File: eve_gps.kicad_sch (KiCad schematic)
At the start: 9 parts, among them J14 BMI-S-101, J15 GNSS SMA

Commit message: Addressed comments; See issue for notes
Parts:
- removed J14: BMI-S-101, RF_Shielding:Laird_Technologies_BMI-S-101_13.66x12.70mm, symbol Device:RFShield_OnePiece
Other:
- note removed: "MURK SHIELD AND MOVE CIRCUIT COSER"
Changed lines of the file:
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@@
-		)
-	)
-	(text "MURK SHIELD AND  MOVE CIRCUIT COSER"
-		(exclude_from_sim no)
-		(at 185.674 117.602 0)
-		(effects
-			(font
-				(size 1.27 1.27)
-				(color 255 0 21 1)
-			)
 		)
 	)
@@
 					(unit 1)
 				)
-			)
-		)
-	)
-	(symbol
-		(lib_id "power:GND")
-		(at 168.91 144.78 0)
-		(unit 1)
-		(exclude_from_sim no)
-		(in_bom yes)
-		(on_board yes)
-		(dnp no)
-		(property "Reference" "#PWR0193"
-			(at 168.91 151.13 0)
-			(effects
-				(font
-					(size 1.27 1.27)
-				)
-				(hide yes)
-			)
-		)
-		(property "Value" "GND"
-			(at 168.91 148.59 0)
-			(effects
-				(font
-					(size 1.27 1.27)
-				)
-			)
-		)
-		(property "Footprint" ""
-			(at 168.91 144.78 0)
-			(effects
-				(font
-					(size 1.27 1.27)
-				)
-				(hide yes)
-			)
-		)
-		(property "Datasheet" ""
-			(at 168.91 144.78 0)
-			(effects
-				(font
-					(size 1.27 1.27)
-				)
-				(hide yes)
-			)
-		)
-		(property "Description" ""
-			(at 168.91 144.78 0)
-			(effects
-				(font
-					(size 1.27 1.27)
-				)
-				(hide yes)
-			)
-		)
-		(pin "1"
-		)
-		(instances
-			(project "rocket2-ecu"
-				(path "/02606b2c-b376-4ffb-9781-f9cea3f70994/33703977-e0e9-46ee-bac6-f4661129caa1"
-					(reference "#PWR0193")
-					(unit 1)
-				)
-			)
-			(project "EVE"
-				(path "/cd9ffd1a-f084-4abb-b7eb-d4533d60a555"
-					(reference "#PWR090")
-					(unit 1)
-				)
-			)
-		)
-	)
-	(symbol
-		(lib_id "Device:RFShield_OnePiece")
-		(at 168.91 134.62 0)
-		(unit 1)
-		(exclude_from_sim no)
-		(in_bom yes)
-		(on_board yes)
-		(dnp no)
-		(property "Reference" "J14"
-			(at 163.83 122.428 0)
-			(effects
-				(font
-					(size 1.27 1.27)
-				)
-				(justify left)
-			)
-		)
-		(property "Value" "BMI-S-101"
-			(at 163.83 124.968 0)
-			(effects
-				(font
-					(size 1.27 1.27)
-				)
-				(justify left)
-			)
-		)
-		(property "Footprint" "RF_Shielding:Laird_Technologies_BMI-S-101_13.66x12.70mm"
-			(at 168.91 137.16 0)
-			(effects
-				(font
-					(size 1.27 1.27)
-				)
-				(hide yes)
-			)
-		)
-		(property "Datasheet" "https://www.laird.com/sites/default/files/bmi-s-101-sales.pdf"
-			(at 168.91 137.16 0)
-			(effects
-				(font
-					(size 1.27 1.27)
-				)
-				(hide yes)
-			)
-		)
-		(property "Description" ""
-			(at 168.91 134.62 0)
-			(effects
-				(font
-					(size 1.27 1.27)
-				)
-				(hide yes)
-			)
-		)
-		(property "Manufacturer" "Laird"
-			(at 168.91 134.62 0)
-			(effects
-				(font
-					(size 1.27 1.27)
-				)
-				(hide yes)
-			)
-		)
-		(property "Part #" "BMI-S-101"
-			(at 168.91 134.62 0)
-			(effects
-				(font
-					(size 1.27 1.27)
-				)
-				(hide yes)
-			)
-		)
-		(pin "1"
-		)
-		(instances
-			(project "rocket2-ecu"
-				(path "/02606b2c-b376-4ffb-9781-f9cea3f70994/33703977-e0e9-46ee-bac6-f4661129caa1"
-					(reference "J14")
-					(unit 1)
-				)
-			)
-			(project "EVE"
-				(path "/cd9ffd1a-f084-4abb-b7eb-d4533d60a555"
-					(reference "J6")
-					(unit 1)
-				)

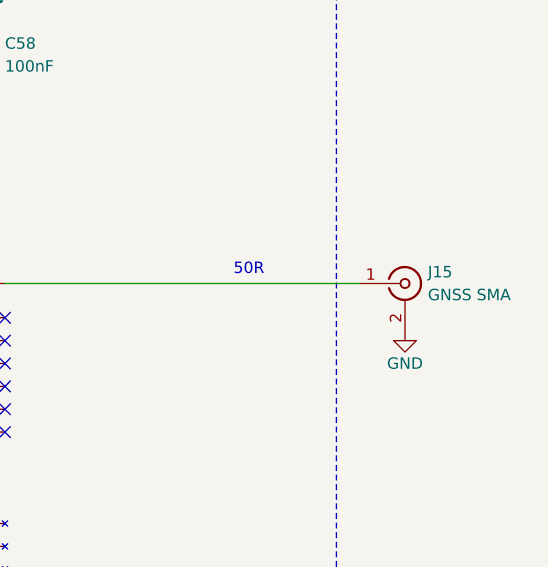
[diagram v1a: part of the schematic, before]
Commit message: REDS updated with diodes and hierarchy to main micro
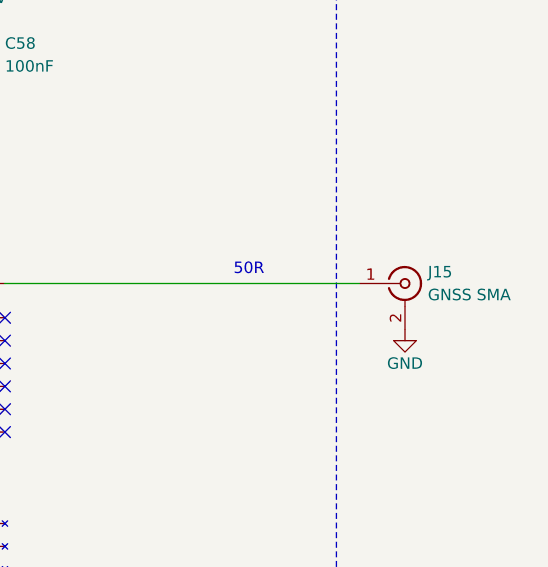
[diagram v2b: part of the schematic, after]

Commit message: layout done
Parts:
- J15: footprint Connector_Coaxial:SMA_Molex_73251-2200_Horizontal -> 0UCIRP-KiCAD-Lib:CONN_73391-0070_MOL
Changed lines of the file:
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@@
 			)
 		)
-		(property "Footprint" "Connector_Coaxial:SMA_Molex_73251-2200_Horizontal"
+		(property "Footprint" "0UCIRP-KiCAD-Lib:CONN_73391-0070_MOL"
 			(at 194.31 86.36 0)
 			(effects
@@
 			)
 		)
-		(property "Datasheet" "https://www.molex.com/en-us/products/part-detail/732512200?display=pdf"
+		(property "Datasheet" "https://www.molex.com/en-us/products/part-detail/733910070?display=pdf"
 			(at 194.31 86.36 0)
 			(effects
